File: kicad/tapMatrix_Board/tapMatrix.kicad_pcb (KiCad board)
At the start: 4 copper layers, 68.6 x 53.3 mm, 65 parts, among them P1 +9V Power, P2 USB-MINI-B, P5 TS_ZIF, P6 LED_MATRIX_HDR, SW1 SW_PUSH, U1 MCP1703, U10 2N7002PW, U2 MCP4921-E/SN, U3 74AHC125, U4 TS922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

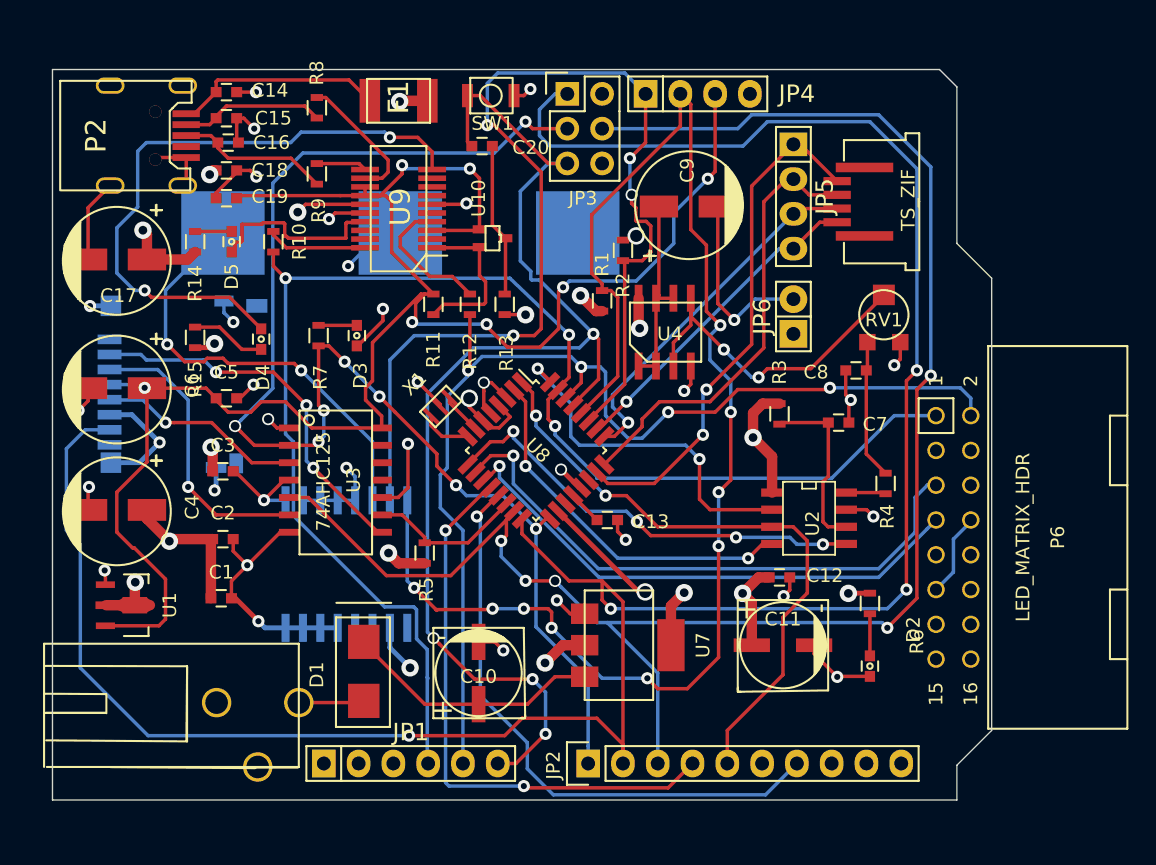
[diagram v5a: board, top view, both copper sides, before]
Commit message: Complete routing and formatting, create Gerbers
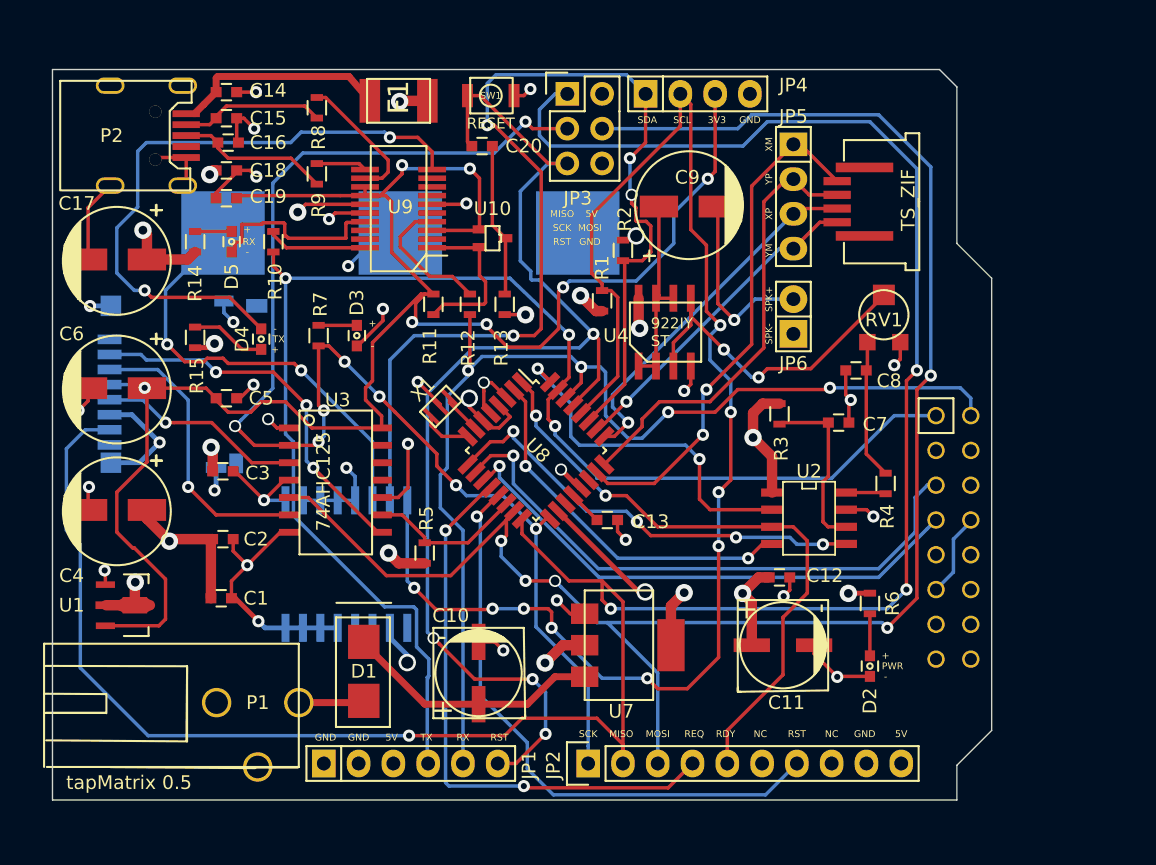
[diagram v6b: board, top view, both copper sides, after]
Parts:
- removed SW1: SW_PUSH, SW_3BU_1000P
- added RESET: SW_PUSH, SW_3BU_1000P, F.Cu at (162.8, 88.3)
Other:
- board text added: "+"
- board text added: "-"
- board text added: "3V3"
- board text added: "922IY ST"
- board text added: "NC"
- board text added: "PWR"
- board text added: "RDY"
- board text added: "REQ"
- board text added: "RX"
- board text added: "SPK+"
- board text added: "SPK-"
- board text added: "SW1"
- board text added: "TX"
- board text added: "XM"
- board text added: "XP"
- board text added: "YM"
- board text added: "YP"
- board text added: "tapMatrix 0.5"
- board text added: "tapMatrix 0.5 Responsive Devices Inc April 2015"
- board text removed: "3.3V"
- board text removed: "Aref"
- board text removed: "INT0"
- board text removed: "INT1/PWM"
- board text removed: "IOref"
- board text removed: "MOSI/PWM"
- board text removed: "PWM"
- board text removed: "Rx"
- board text removed: "SCK/LED"
- board text removed: "SS/PWM"
- board text removed: "Tx"
- board text removed: "VTG"
- board text removed: "Vin"
